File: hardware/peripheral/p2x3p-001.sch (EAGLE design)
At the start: 4 parts, among them J4 RLY

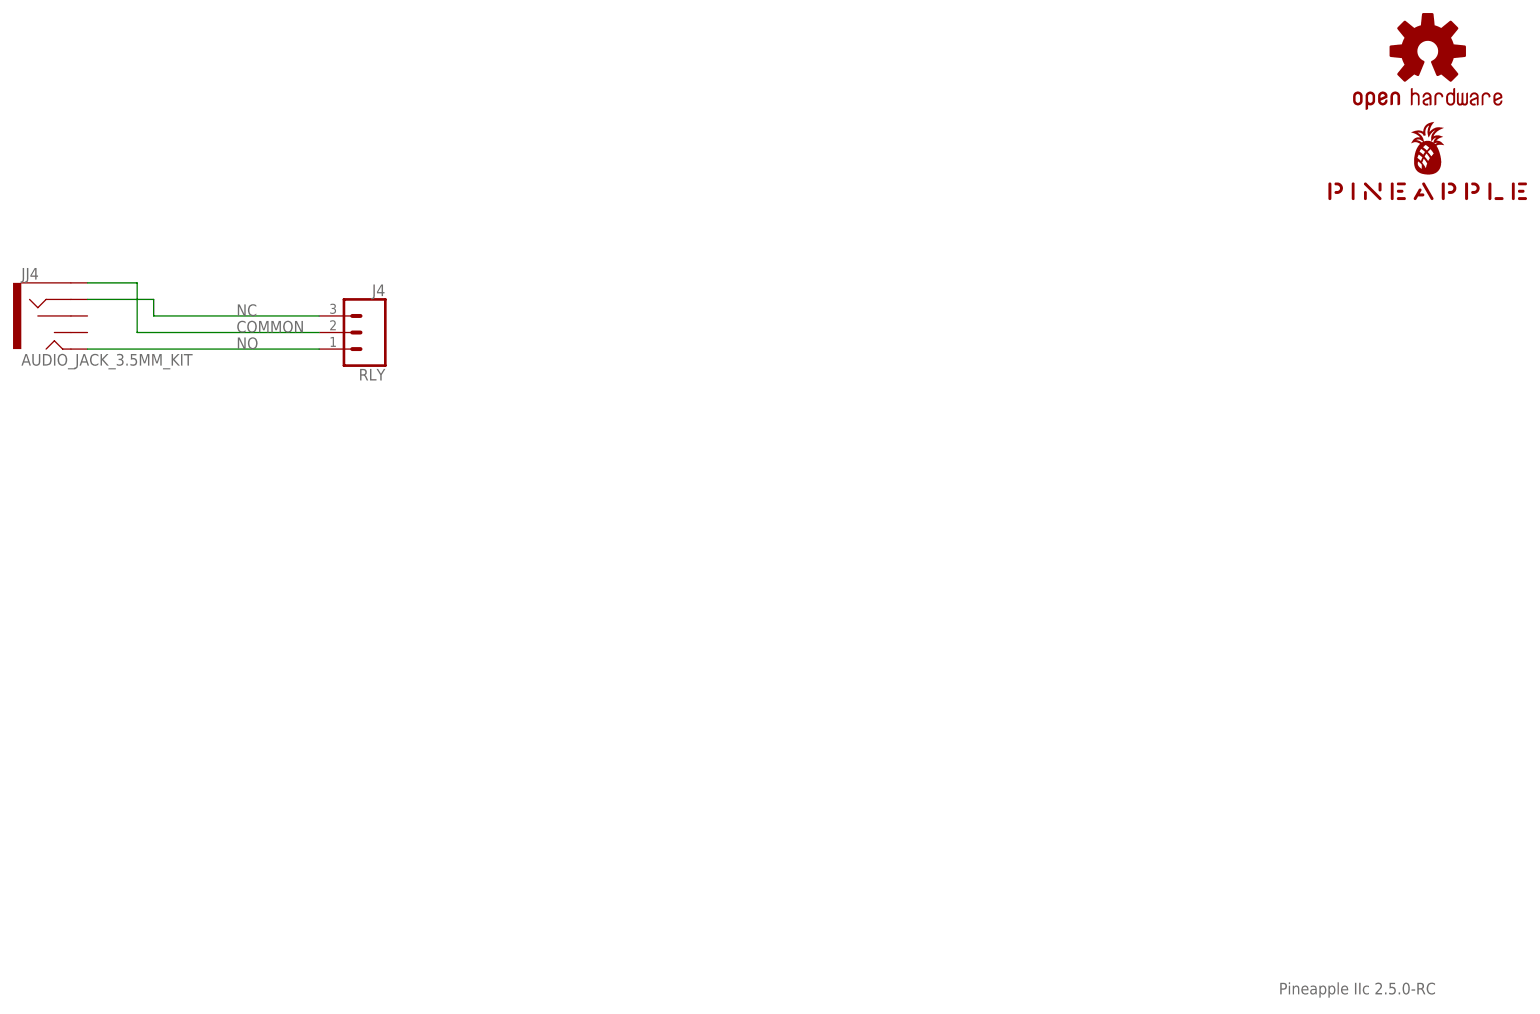
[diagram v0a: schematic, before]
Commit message: Imported (again) from Hex Sw 0.0.2-X.
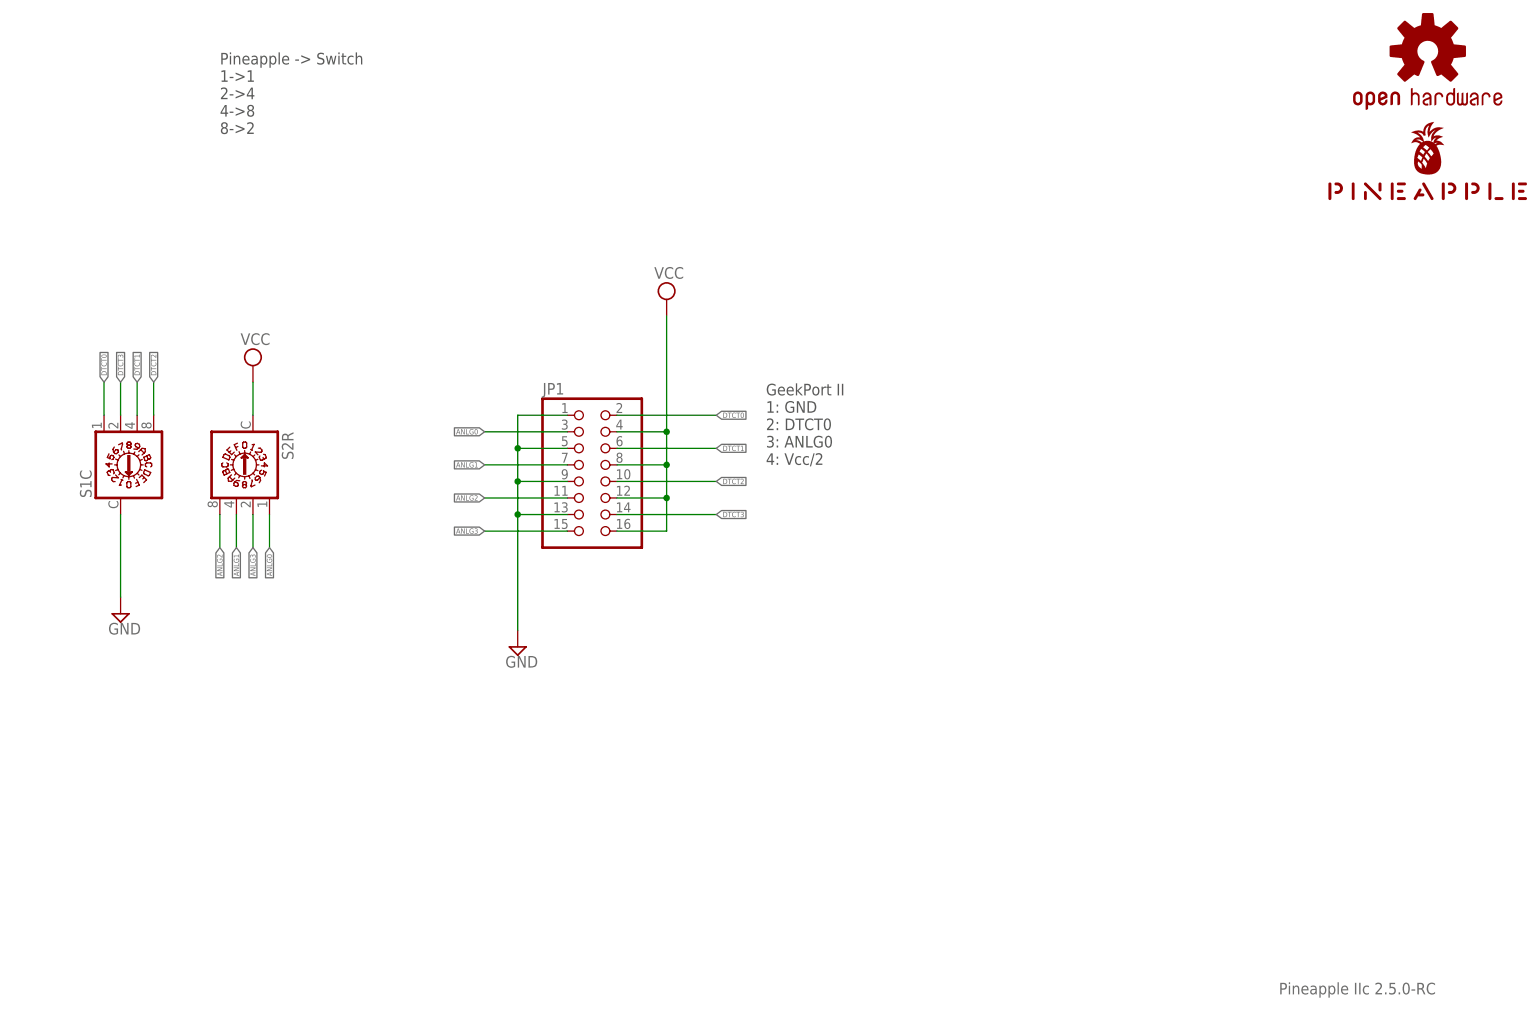
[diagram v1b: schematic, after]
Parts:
- removed J4: RLY, SparkFun-Connectors:CONN_03JST-PTH-VERT
- removed JJ4: AUDIO_JACK_3.5MM_KIT, SparkFun-Connectors:AUDIO_JACK_3.5MM_KIT
- added JP1: (no value), pinhead:PINHD-2X8
- added S1C, S2R: (no value), switch-dil:A1353HEX
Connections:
- removed net COMMON: J4.2, JJ4.SLEEVE
- removed net NC: J4.3, JJ4.RING
- removed net NO: J4.1, JJ4.TIP
- new net ANLG0: JP1.3, S2R.1
- new net ANLG1: JP1.7, S2R.4
- new net ANLG2: JP1.11, S2R.8
- new net ANLG3: JP1.15, S2R.2
- new net DTCT0: JP1.2, S1C.1
- new net DTCT1: JP1.6, S1C.4
- new net DTCT2: JP1.10, S1C.8
- new net DTCT3: JP1.14, S1C.2
- new net GND: JP1.1, JP1.13, JP1.5, JP1.9, S1C.C
- new net VCC: JP1.12, JP1.16, JP1.4, JP1.8, S2R.C
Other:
- note added: "GeekPort II 1: GND 2: DTCT0 3: ANLG0 4: Vcc/2"
- note added: "Pineapple -> Switch 1->1 2->4 4->8 8->2"

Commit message: WIP.
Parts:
- removed S1C, S2R: (no value), switch-dil:A1353HEX
- added J1, J2: (no value), SparkFun-Connectors:CONN_03JST-PTH
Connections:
- net ANLG0: no longer S2R.1
- net ANLG1: no longer S2R.4
- net ANLG2: no longer S2R.8
- net ANLG3: no longer S2R.2
- net DTCT0: no longer S1C.1
- net DTCT1: no longer S1C.4
- net DTCT2: no longer S1C.8
- net DTCT3: no longer S1C.2
- net GND: no longer S1C.C
- net VCC: no longer S2R.C
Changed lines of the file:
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@@
 <part name="LOGO1" library="SparkFun-Aesthetics" deviceset="OSHW-LOGO" device="S-COPPER" value="OSHW-LOGOS-COPPER"/>
 <part name="JP1" library="pinhead" library_urn="urn:adsk.eagle:library:325" deviceset="PINHD-2X8" device="" package3d_urn="urn:adsk.eagle:package:22481/2"/>
-<part name="S1C" library="switch-dil" library_urn="urn:adsk.eagle:library:375" deviceset="A1353HEX" device="" package3d_urn="urn:adsk.eagle:package:27207/1"/>
-<part name="S2R" library="switch-dil" library_urn="urn:adsk.eagle:library:375" deviceset="A1353HEX" device="" package3d_urn="urn:adsk.eagle:package:27207/1"/>
 <part name="SUPPLY1" library="supply2" library_urn="urn:adsk.eagle:library:372" deviceset="GND" device=""/>
-<part name="SUPPLY2" library="supply2" library_urn="urn:adsk.eagle:library:372" deviceset="GND" device=""/>
 <part name="SUPPLY3" library="supply2" library_urn="urn:adsk.eagle:library:372" deviceset="VCC" device=""/>
-<part name="SUPPLY4" library="supply2" library_urn="urn:adsk.eagle:library:372" deviceset="VCC" device=""/>
 <part name="U$1" library="pineapple" deviceset="PINEAPPLE450_SILK" device=""/>
+<part name="J1" library="SparkFun-Connectors" library_urn="urn:adsk.eagle:library:513" deviceset="CONN_03" device="JST-PTH" package3d_urn="urn:adsk.eagle:package:38069/1"/>
+<part name="J2" library="SparkFun-Connectors" library_urn="urn:adsk.eagle:library:513" deviceset="CONN_03" device="JST-PTH" package3d_urn="urn:adsk.eagle:package:38069/1"/>
 </parts>
 <sheets>
@@
 <attribute name="VALUE" x="105.41" y="86.36" size="1.778" layer="96"/>
 </instance>
-<instance part="S1C" gate="1" x="40.64" y="101.6" smashed="yes">
-<attribute name="NAME" x="36.195" y="96.52" size="1.778" layer="95" rot="R90"/>
-<attribute name="VALUE" x="49.53" y="96.52" size="1.778" layer="96" rot="R90"/>
-</instance>
-<instance part="S2R" gate="1" x="60.96" y="101.6" smashed="yes" rot="R180">
-<attribute name="NAME" x="65.405" y="106.68" size="1.778" layer="95" rot="R270"/>
-<attribute name="VALUE" x="52.07" y="106.68" size="1.778" layer="96" rot="R270"/>
-</instance>
 <instance part="SUPPLY1" gate="GND" x="101.6" y="73.66" smashed="yes">
 <attribute name="VALUE" x="99.695" y="70.485" size="1.778" layer="96"/>
-</instance>
-<instance part="SUPPLY2" gate="GND" x="40.64" y="78.74" smashed="yes">
-<attribute name="VALUE" x="38.735" y="75.565" size="1.778" layer="96"/>
 </instance>
 <instance part="SUPPLY3" gate="G$1" x="124.46" y="127" smashed="yes">
 <attribute name="VALUE" x="122.555" y="130.175" size="1.778" layer="96"/>
 </instance>
-<instance part="SUPPLY4" gate="G$1" x="60.96" y="116.84" smashed="yes">
-<attribute name="VALUE" x="59.055" y="120.015" size="1.778" layer="96"/>
+<instance part="U$1" gate="G$1" x="241.3" y="142.24" smashed="yes"/>
+<instance part="J1" gate="J$1" x="63.5" y="109.22" smashed="yes">
+<attribute name="VALUE" x="60.96" y="101.854" size="1.778" layer="96" font="vector"/>
+<attribute name="NAME" x="60.96" y="114.808" size="1.778" layer="95" font="vector"/>
 </instance>
-<instance part="U$1" gate="G$1" x="241.3" y="142.24" smashed="yes"/>
+<instance part="J2" gate="J$1" x="63.5" y="96.52" smashed="yes">
+<attribute name="VALUE" x="60.96" y="89.154" size="1.778" layer="96" font="vector"/>
+<attribute name="NAME" x="60.96" y="102.108" size="1.778" layer="95" font="vector"/>
+</instance>
 </instances>
 <busses>
@@
 <junction x="101.6" y="93.98"/>
 </segment>
-<segment>
-<pinref part="S1C" gate="1" pin="C"/>
-<wire x1="40.64" y1="93.98" x2="40.64" y2="81.28" width="0.1524" layer="91"/>
-<pinref part="SUPPLY2" gate="GND" pin="GND"/>
-</segment>
 </net>
 <net name="DTCT0" class="0">
@@
 <wire x1="116.84" y1="109.22" x2="132.08" y2="109.22" width="0.1524" layer="91"/>
 <label x="132.08" y="109.22" size="0.8128" layer="95" xref="yes"/>
-</segment>
-<segment>
-<pinref part="S1C" gate="1" pin="1"/>
-<wire x1="38.1" y1="109.22" x2="38.1" y2="114.3" width="0.1524" layer="91"/>
-<label x="38.1" y="114.3" size="0.8128" layer="95" rot="R90" xref="yes"/>
 </segment>
 </net>
@@
 <junction x="124.46" y="101.6"/>
 </segment>
-<segment>
-<pinref part="S2R" gate="1" pin="C"/>
-<wire x1="60.96" y1="109.22" x2="60.96" y2="114.3" width="0.1524" layer="91"/>
-<pinref part="SUPPLY4" gate="G$1" pin="VCC"/>
-</segment>
 </net>
 <net name="DTCT1" class="0">
@@
 <wire x1="116.84" y1="104.14" x2="132.08" y2="104.14" width="0.1524" layer="91"/>
 <label x="132.08" y="104.14" size="0.8128" layer="95" xref="yes"/>
-</segment>
-<segment>
-<pinref part="S1C" gate="1" pin="4"/>
-<wire x1="43.18" y1="109.22" x2="43.18" y2="114.3" width="0.1524" layer="91"/>
-<label x="43.18" y="114.3" size="0.8128" layer="95" rot="R90" xref="yes"/>
 </segment>
 </net>
@@
 <label x="132.08" y="99.06" size="0.8128" layer="95" xref="yes"/>
 </segment>
-<segment>
-<pinref part="S1C" gate="1" pin="8"/>
-<wire x1="45.72" y1="109.22" x2="45.72" y2="114.3" width="0.1524" layer="91"/>
-<label x="45.72" y="114.3" size="0.8128" layer="95" rot="R90" xref="yes"/>
-</segment>
 </net>
 <net name="DTCT3" class="0">
@@
 <wire x1="116.84" y1="93.98" x2="132.08" y2="93.98" width="0.1524" layer="91"/>
 <label x="132.08" y="93.98" size="0.8128" layer="95" xref="yes"/>
-</segment>
-<segment>
-<pinref part="S1C" gate="1" pin="2"/>
-<wire x1="40.64" y1="109.22" x2="40.64" y2="114.3" width="0.1524" layer="91"/>
-<label x="40.64" y="114.3" size="0.8128" layer="95" rot="R90" xref="yes"/>
 </segment>
 </net>
@@
 <label x="96.52" y="106.68" size="0.8128" layer="95" rot="R180" xref="yes"/>
 </segment>
-<segment>
-<pinref part="S2R" gate="1" pin="1"/>
-<wire x1="63.5" y1="93.98" x2="63.5" y2="88.9" width="0.1524" layer="91"/>
-<label x="63.5" y="88.9" size="0.8128" layer="95" rot="R270" xref="yes"/>
-</segment>
 </net>
 <net name="ANLG1" class="0">
@@
 <label x="96.52" y="101.6" size="0.8128" layer="95" rot="R180" xref="yes"/>
 </segment>
-<segment>
-<pinref part="S2R" gate="1" pin="4"/>
-<wire x1="58.42" y1="93.98" x2="58.42" y2="88.9" width="0.1524" layer="91"/>
-<label x="58.42" y="88.9" size="0.8128" layer="95" rot="R270" xref="yes"/>
-</segment>
 </net>
 <net name="ANLG3" class="0">
-<segment>
-<pinref part="S2R" gate="1" pin="2"/>
-<wire x1="60.96" y1="93.98" x2="60.96" y2="88.9" width="0.1524" layer="91"/>
-<label x="60.96" y="88.9" size="0.8128" layer="95" rot="R270" xref="yes"/>
-</segment>
 <segment>
 <pinref part="JP1" gate="A" pin="15"/>
@@
 <net name="ANLG2" class="0">
 <segment>
-<pinref part="S2R" gate="1" pin="8"/>
-<wire x1="55.88" y1="93.98" x2="55.88" y2="88.9" width="0.1524" layer="91"/>
-<label x="55.88" y="88.9" size="0.8128" layer="95" rot="R270" xref="yes"/>
-</segment>
-<segment>
 <pinref part="JP1" gate="A" pin="11"/>
